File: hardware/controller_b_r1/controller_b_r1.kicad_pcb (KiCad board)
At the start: 2 copper layers, 131.5 x 12.9 mm, 54 parts, among them J101 Front Pannel Connector, J102 SWD Header, J103 USB Micro B, Q101 NMOS, SW101 Reset Button, SW102 User Button, U101 NCP115ASN330T2G, U102 74LVC2T45HK3, U103 RP2040, U104 W25Q16JVUXIQ, Y101 12MHz

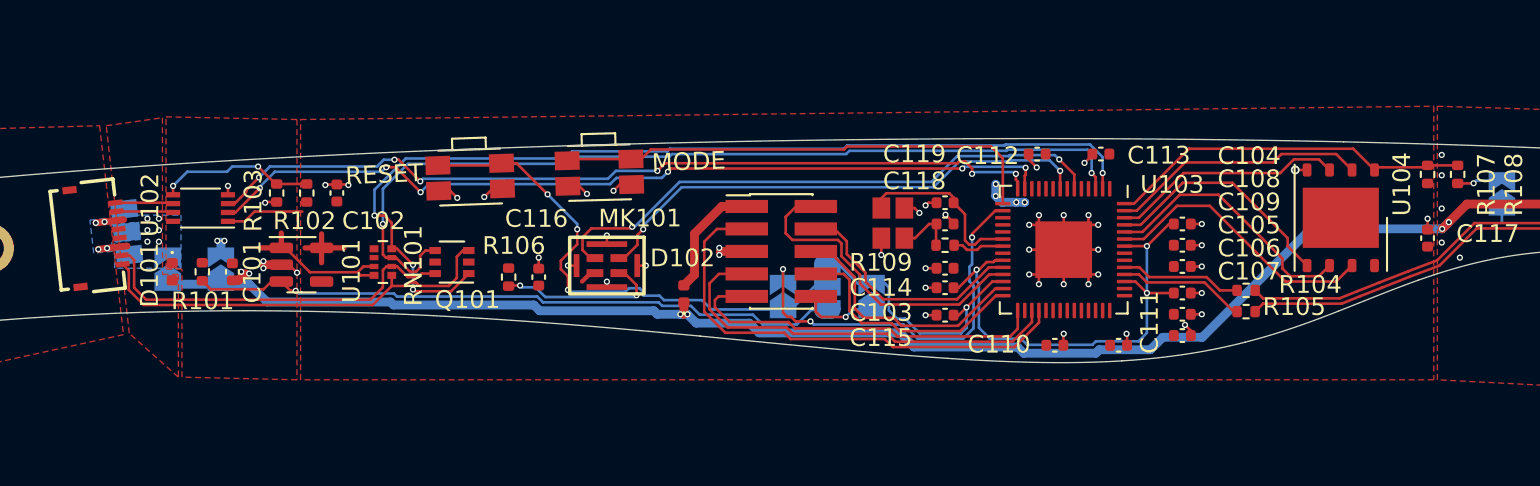
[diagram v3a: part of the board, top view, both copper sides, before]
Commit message: First pass at the rev 2 power board.
Only did copper layers on the power board so far. Waiting to decide on a PCB fab house then I'll go back and make sure it's compliant (looking mostly at how close I can pack vias). Starting on the nucleo programmer shield next. Added a voltage divider to the enable pin on the 3V3 vreg on the controller board so it only switches on when there is enough input voltage for correct 3V3 output. I did this because I read somewhere that the RP2040 can power on at a lower voltage than a lot of flash chips and if that happens it gets into a weird state so I'm trying to make sure 3V3 comes on as quickly and sharply as possible.
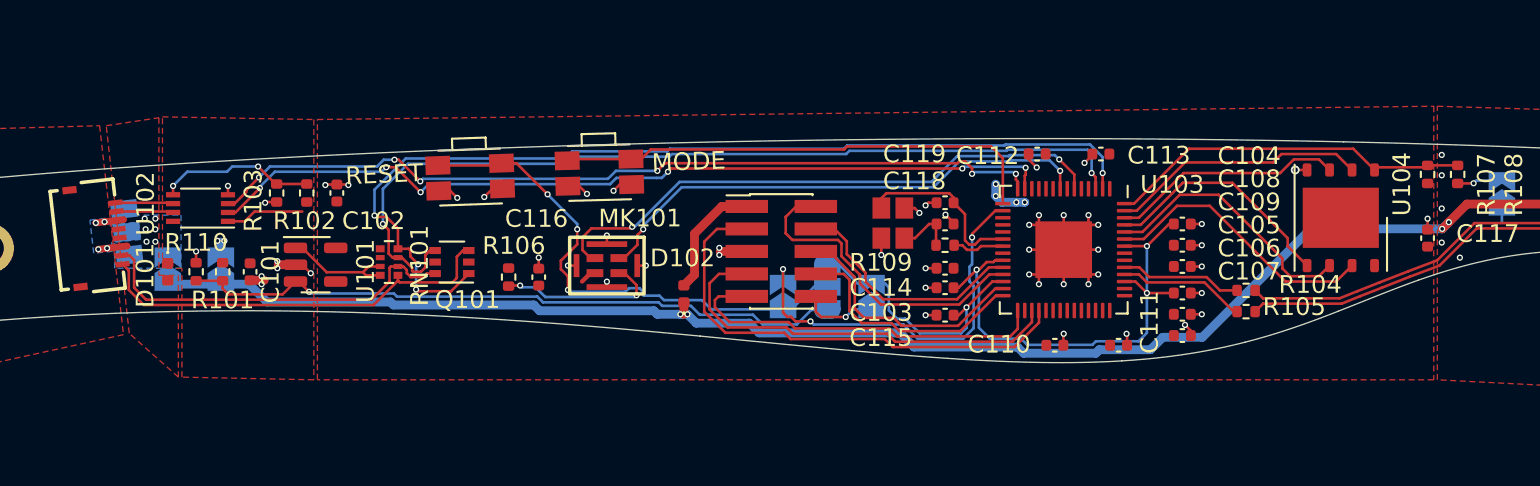
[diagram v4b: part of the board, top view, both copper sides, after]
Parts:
- added R110: 15k, Resistor_SMD:R_0402_1005Metric, F.Cu at (117.3, 107.7)
- R101: value 10k -> 75k
- moved R101 1.15 mm to (118.8, 107.7)
- moved C101 1.00 mm to (120.3, 107.7)
- moved U101 0.80 mm to (124.0, 107.3)
- moved RN101 0.35 mm to (128.2, 107.2)
- moved D101 0.25 mm to (115.7, 107.7)
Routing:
- net +3V3: track 11.6 -> 7.81 mm
- net +5V: track 9.34 -> 6.89 mm
- net /3V3_EN: track 37.0 -> 37.9 mm
- net GND: track 56.0 -> 56.6 mm, vias 67 -> 68

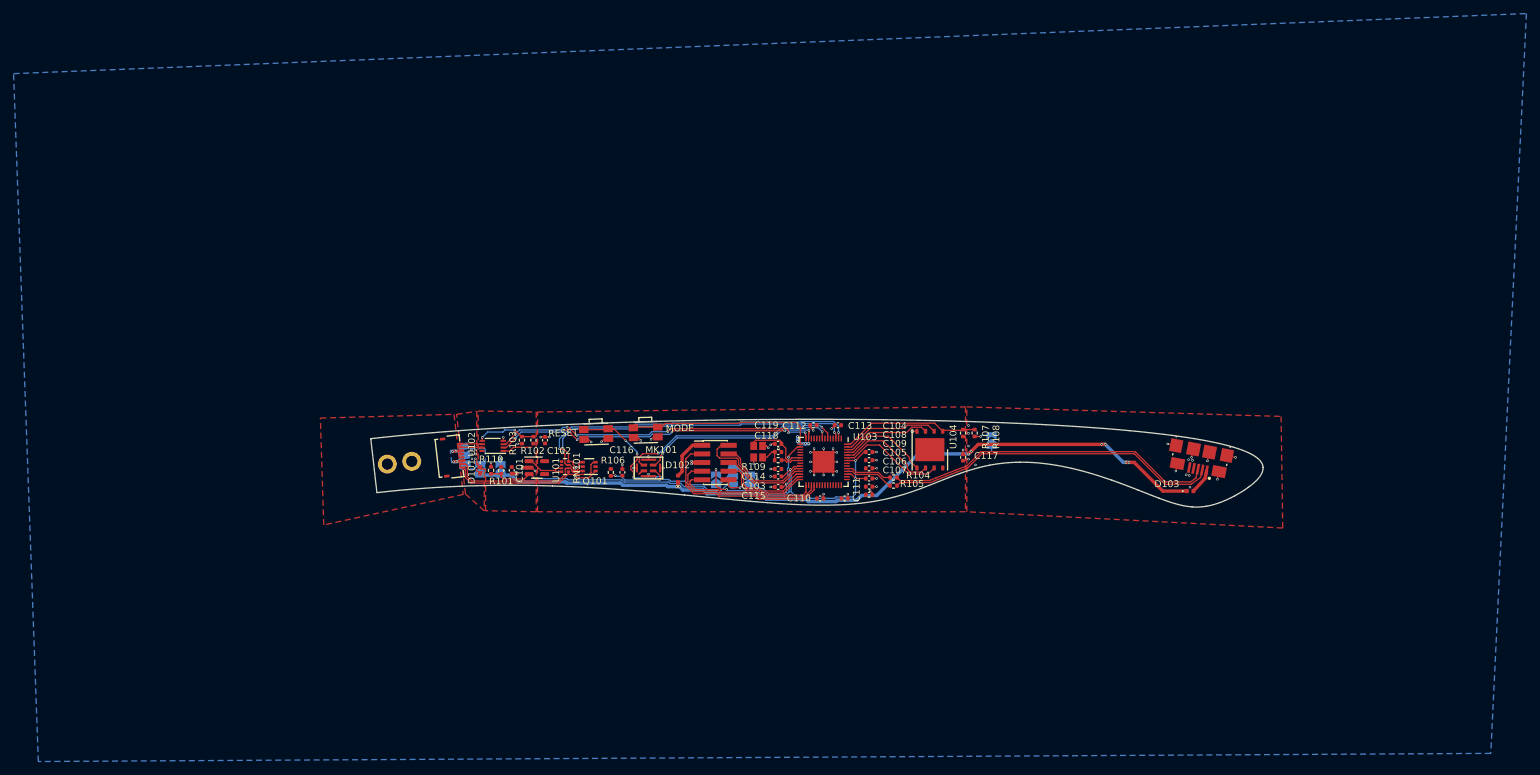
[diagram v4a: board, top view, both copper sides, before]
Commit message: Next revision of the boards are finished and ready for fabrication, and a BOM has been added.
The BOM is still missing components for the nucleo shield.
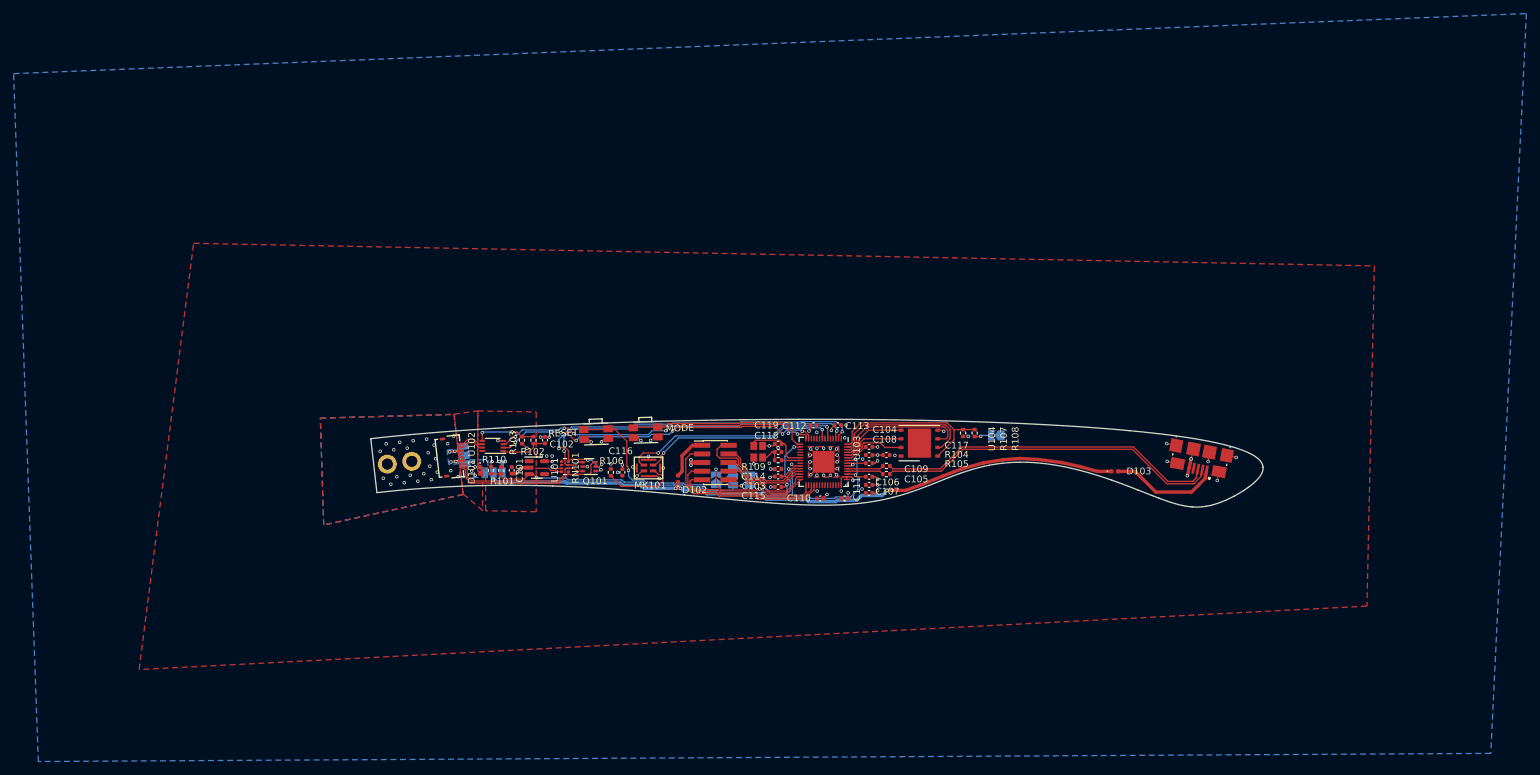
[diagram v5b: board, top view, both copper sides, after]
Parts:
- removed JP103: SolderJumper_2_Open, Jumper:SolderJumper-2_P1.3mm_Open_TrianglePad1.0x1.5mm
- JP102: value SolderJumper_2_Open -> SolderJumper_3_Open; footprint Jumper:SolderJumper-2_P1.3mm_Open_TrianglePad1.0x1.5mm -> rave_shades:SolderJumper-3_P1.3mm_Open_Pad1.0x1.5mm
- JP104: footprint Jumper:SolderJumper-3_P1.3mm_Open_RoundedPad1.0x1.5mm -> rave_shades:SolderJumper-3_P1.3mm_Open_Pad1.0x1.5mm
- JP107: footprint Jumper:SolderJumper-3_P1.3mm_Open_Pad1.0x1.5mm -> rave_shades:SolderJumper-3_P1.3mm_Open_Pad1.0x1.5mm
- SW101: value Reset Button -> User Button
- moved D103 11.5 mm to (209.2, 107.8)
- moved C117 11.3 mm to (175.6, 105.5), turned to 180 degrees
- moved JP102 2.00 mm to (117.7, 108.0), turned to 180 degrees
- moved R104 2.00 mm to (175.6, 107.0)
- moved R105 2.00 mm to (175.6, 108.2)
- moved U104 1.81 mm to (180.4, 103.7), turned to 180 degrees
- moved JP106 1.03 mm to (191.8, 102.5), turned to 180 degrees
- moved C104 0.75 mm to (173.0, 104.2)
- moved C108 0.75 mm to (173.0, 105.5)
- moved C109 0.75 mm to (173.0, 106.7)
- moved C105 0.25 mm to (173.0, 108.7)
- moved C106 0.25 mm to (173.0, 109.8)
- moved C107 0.25 mm to (173.0, 111.0)
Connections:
- J101 pad 9: GND -> unconnected-(J101-Pad9)
- JP102 pad 1: VBUS -> +5V
- JP102 pad 2: VDD -> VBUS
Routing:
- net VBUS: track 114.3 -> 97.4 mm, vias 8 -> 4
- net GND: track 56.6 -> 72.0 mm, vias 68 -> 82
- net /VDD_USB: track 3.66 -> 16.0 mm
- net +3V3: track 7.81 -> 17.6 mm, vias 4 -> 24
- net /FLASH_IO1: track 14.5 -> 21.4 mm
- net /FLASH_IO2: track 13.2 -> 19.6 mm
- net /FLASH_IO3: track 15.8 -> 9.36 mm
- net /FLASH_CLK: track 14.9 -> 9.27 mm
- net /FLASH_nCS: track 20.7 -> 26.3 mm
- net /FLASH_IO0: track 13.5 -> 9.73 mm
- net /USB_D_TERM_N: track 7.22 -> 5.49 mm
- net /USB_D_TERM_P: track 6.89 -> 5.49 mm
- net /USB_D_P: track 48.9 -> 50.3 mm
- net /MIC_SELECT: track 9.40 -> 10.8 mm, vias 2 -> 0
- net /USB_D_N: track 49.5 -> 50.9 mm
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- added copper zone on In2.Cu, net +3V3
- added copper zone on In1.Cu, net GND
- added copper zone on In2.Cu, net GND
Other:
- copper layers 2 -> 4
- board text added: "1.5A"
- board text added: "3A"
- board text added: "ANOTHER LAMAL AND DARDY CREATION"
- board text added: "CONTROLLER B REV 1"
- board text added: "PASS THROUGH"
- board text removed: "PASS THR- OUGH"
- board text removed: "PWR SEL"
- board text removed: "VDD+GND CABLE SEL JUST VDD"

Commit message: Updated kicad files to work with latest kicad. Added some todos for next hw design.
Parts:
- U102: value 74LVC2T45HK3 -> 74LVCH2T45DC,125
- U104: value W25Q16JVUXIQ -> W25Q16JVZPIQ
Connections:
- J101 pad 9: unconnected-(J101-Pad9) -> (no net)
- J103 pad 4: unconnected-(J103-Pad4) -> (no net)
- U103 pad 11: unconnected-(U103-Pad11) -> (no net)
- U103 pad 12: unconnected-(U103-Pad12) -> (no net)
- U103 pad 17: unconnected-(U103-Pad17) -> (no net)
- U103 pad 18: unconnected-(U103-Pad18) -> (no net)
- U103 pad 19: unconnected-(U103-Pad19) -> (no net)
- U103 pad 30: unconnected-(U103-Pad30) -> (no net)
- U103 pad 34: unconnected-(U103-Pad34) -> (no net)
- U103 pad 35: unconnected-(U103-Pad35) -> (no net)
- U103 pad 36: unconnected-(U103-Pad36) -> (no net)
- U103 pad 37: unconnected-(U103-Pad37) -> (no net)
- U103 pad 38: unconnected-(U103-Pad38) -> (no net)
- U103 pad 39: unconnected-(U103-Pad39) -> (no net)
- U103 pad 4: unconnected-(U103-Pad4) -> (no net)
- U103 pad 40: unconnected-(U103-Pad40) -> (no net)
- U103 pad 41: unconnected-(U103-Pad41) -> (no net)
- U103 pad 5: unconnected-(U103-Pad5) -> (no net)
- U103 pad 7: unconnected-(U103-Pad7) -> (no net)
- U103 pad 9: unconnected-(U103-Pad9) -> (no net)
- U104 pad 9: unconnected-(U104-Pad9) -> (no net)
